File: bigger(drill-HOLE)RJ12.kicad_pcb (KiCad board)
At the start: 2 copper layers, 21.6 x 27.9 mm, 2 parts, among them J1 Conn_02x06_Top_Bottom, P1 RJ12_Housing

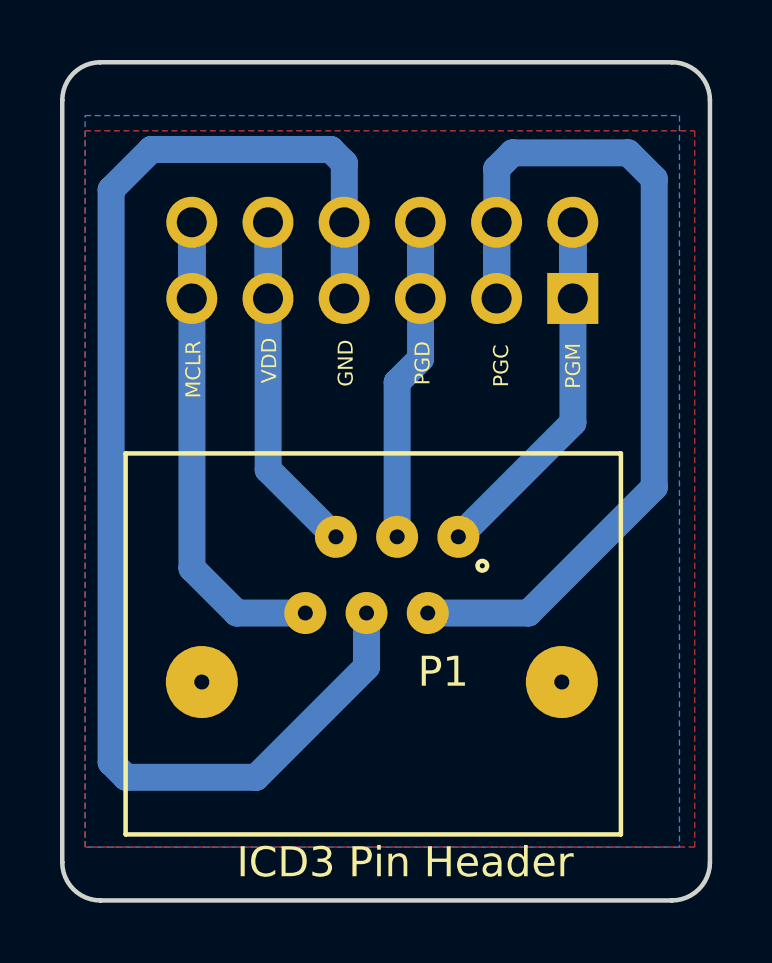
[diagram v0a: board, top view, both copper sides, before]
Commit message: Re-design the rj12 housing
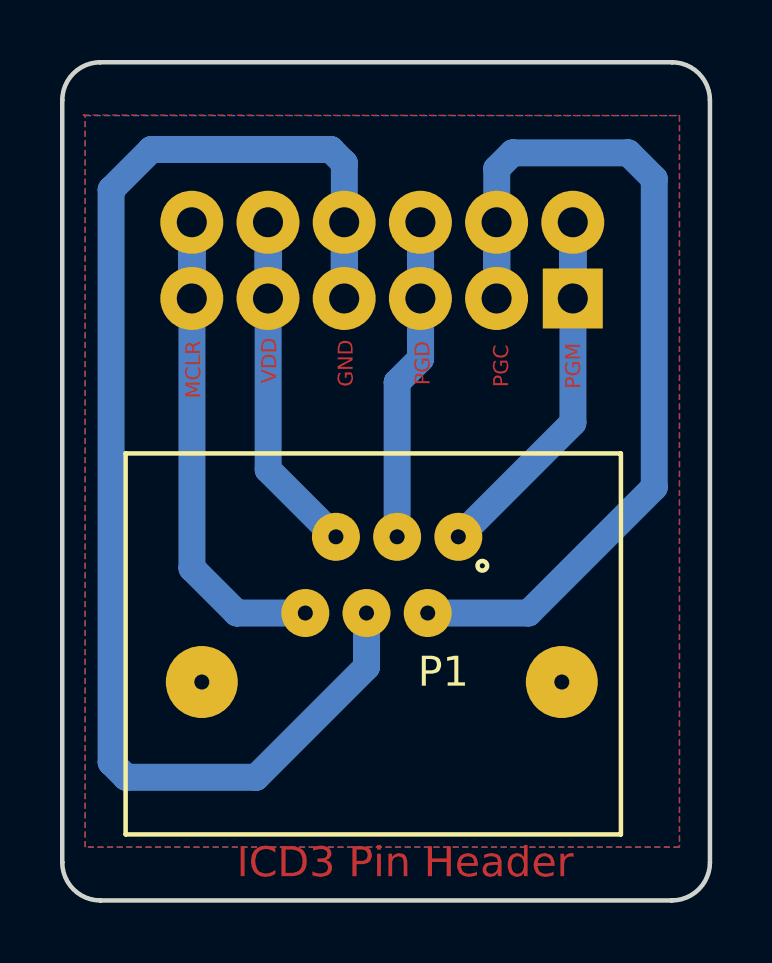
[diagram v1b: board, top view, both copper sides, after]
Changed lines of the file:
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@@
   (page A4)
   (layers
-    (0 F.Cu signal hide)
+    (0 F.Cu signal)
     (31 B.Cu signal)
     (32 B.Adhes user)
@@
     (mod_text_size 1 1)
     (mod_text_width 0.15)
-    (pad_size 1.7 1.7)
-    (pad_drill 1)
+    (pad_size 1.6 1.6)
+    (pad_drill 0.5)
     (pad_to_mask_clearance 0.2)
     (aux_axis_origin 44.45 16.51)
@@
     (pad "" np_thru_hole circle (at 8.55 2.3) (size 2.4 2.4) (drill 0.5) (layers *.Cu *.Mask))
     (pad "" np_thru_hole circle (at -3.45 2.3) (size 2.4 2.4) (drill 0.5) (layers *.Cu *.Mask))
-    (pad 1 thru_hole circle (at 5.1 -2.54) (size 1.4 1.4) (drill 0.5) (layers *.Cu *.Mask)
+    (pad 1 thru_hole circle (at 5.1 -2.54) (size 1.6 1.6) (drill 0.5) (layers *.Cu *.Mask)
       (net 6 pin1))
-    (pad 3 thru_hole circle (at 3.06 -2.54) (size 1.4 1.4) (drill 0.5) (layers *.Cu *.Mask)
+    (pad 3 thru_hole circle (at 3.06 -2.54) (size 1.6 1.6) (drill 0.5) (layers *.Cu *.Mask)
       (net 4 pin3))
-    (pad 5 thru_hole circle (at 1.02 -2.54) (size 1.4 1.4) (drill 0.5) (layers *.Cu *.Mask)
+    (pad 5 thru_hole circle (at 1.02 -2.54) (size 1.6 1.6) (drill 0.5) (layers *.Cu *.Mask)
       (net 1 pin5))
-    (pad 2 thru_hole circle (at 4.08 0) (size 1.4 1.4) (drill 0.5) (layers *.Cu *.Mask)
+    (pad 2 thru_hole circle (at 4.08 0) (size 1.6 1.6) (drill 0.5) (layers *.Cu *.Mask)
       (net 5 pin2))
-    (pad 4 thru_hole circle (at 2.04 0) (size 1.4 1.4) (drill 0.5) (layers *.Cu *.Mask)
+    (pad 4 thru_hole circle (at 2.04 0) (size 1.6 1.6) (drill 0.5) (layers *.Cu *.Mask)
       (net 3 pin4))
-    (pad 6 thru_hole circle (at 0 0) (size 1.4 1.4) (drill 0.5) (layers *.Cu *.Mask)
+    (pad 6 thru_hole circle (at 0 0) (size 1.6 1.6) (drill 0.5) (layers *.Cu *.Mask)
       (net 2 pin6))
   )
@@
       (effects (font (size 1 1) (thickness 0.15)) (justify mirror))
     )
-    (pad 1 thru_hole rect (at 0 0 90) (size 1.7 1.7) (drill 1) (layers *.Cu *.Mask)
+    (pad 1 thru_hole rect (at 0 0 90) (size 2 2) (drill 1) (layers *.Cu *.Mask)
       (net 6 pin1))
-    (pad 7 thru_hole oval (at 2.54 0 90) (size 1.7 1.7) (drill 1) (layers *.Cu *.Mask)
+    (pad 7 thru_hole oval (at 2.54 0 90) (size 2.1 2.1) (drill 1) (layers *.Cu *.Mask)
       (net 6 pin1))
-    (pad 2 thru_hole oval (at 0 -2.54 90) (size 1.7 1.7) (drill 1) (layers *.Cu *.Mask)
+    (pad 2 thru_hole oval (at 0 -2.54 90) (size 2.1 2.1) (drill 1) (layers *.Cu *.Mask)
       (net 5 pin2))
-    (pad 8 thru_hole oval (at 2.54 -2.54 90) (size 1.7 1.7) (drill 1) (layers *.Cu *.Mask)
+    (pad 8 thru_hole oval (at 2.54 -2.54 90) (size 2.1 2.1) (drill 1) (layers *.Cu *.Mask)
       (net 5 pin2))
-    (pad 3 thru_hole oval (at 0 -5.08 90) (size 1.7 1.7) (drill 1) (layers *.Cu *.Mask)
+    (pad 3 thru_hole oval (at 0 -5.08 90) (size 2.1 2.1) (drill 1) (layers *.Cu *.Mask)
       (net 4 pin3))
-    (pad 9 thru_hole oval (at 2.54 -5.08 90) (size 1.7 1.7) (drill 1) (layers *.Cu *.Mask)
+    (pad 9 thru_hole oval (at 2.54 -5.08 90) (size 2.1 2.1) (drill 1) (layers *.Cu *.Mask)
       (net 4 pin3))
-    (pad 4 thru_hole oval (at 0 -7.62 90) (size 1.7 1.7) (drill 1) (layers *.Cu *.Mask)
+    (pad 4 thru_hole oval (at 0 -7.62 90) (size 2.1 2.1) (drill 1) (layers *.Cu *.Mask)
       (net 3 pin4))
-    (pad 10 thru_hole oval (at 2.54 -7.62 90) (size 1.7 1.7) (drill 1) (layers *.Cu *.Mask)
+    (pad 10 thru_hole oval (at 2.54 -7.62 90) (size 2.1 2.1) (drill 1) (layers *.Cu *.Mask)
       (net 3 pin4))
-    (pad 5 thru_hole oval (at 0 -10.16 90) (size 1.7 1.7) (drill 1) (layers *.Cu *.Mask)
+    (pad 5 thru_hole oval (at 0 -10.16 90) (size 2.1 2.1) (drill 1) (layers *.Cu *.Mask)
       (net 1 pin5))
-    (pad 11 thru_hole oval (at 2.54 -10.16 90) (size 1.7 1.7) (drill 1) (layers *.Cu *.Mask)
+    (pad 11 thru_hole oval (at 2.54 -10.16 90) (size 2.1 2.1) (drill 1) (layers *.Cu *.Mask)
       (net 1 pin5))
-    (pad 6 thru_hole oval (at 0 -12.7 90) (size 1.7 1.7) (drill 1) (layers *.Cu *.Mask)
+    (pad 6 thru_hole oval (at 0 -12.7 90) (size 2.1 2.1) (drill 1) (layers *.Cu *.Mask)
       (net 2 pin6))
-    (pad 12 thru_hole oval (at 2.54 -12.7 90) (size 1.7 1.7) (drill 1) (layers *.Cu *.Mask)
+    (pad 12 thru_hole oval (at 2.54 -12.7 90) (size 2.1 2.1) (drill 1) (layers *.Cu *.Mask)
       (net 2 pin6))
     (model ${KISYS3DMOD}/Pin_Headers.3dshapes/Pin_Header_Straight_2x06_Pitch2.54mm.wrl
@@
     )
   )
-  (gr_text MCLR (at 25.96 26.75 90) (layer F.SilkS)
-    (effects (font (size 0.5 0.5) (thickness 0.125)))
-  )
-  (gr_text VDD (at 28.49 26.45 90) (layer F.SilkS)
-    (effects (font (size 0.5 0.5) (thickness 0.125)))
-  )
-  (gr_text GND (at 31.04 26.54 90) (layer F.SilkS)
-    (effects (font (size 0.5 0.5) (thickness 0.125)))
-  )
-  (gr_text PGD (at 33.6 26.54 90) (layer F.SilkS)
-    (effects (font (size 0.5 0.5) (thickness 0.125)))
-  )
-  (gr_text PGC (at 36.22 26.63 90) (layer F.SilkS)
-    (effects (font (size 0.5 0.5) (thickness 0.125)))
-  )
-  (gr_text PGM (at 38.62 26.63 90) (layer F.SilkS)
-    (effects (font (size 0.5 0.5) (thickness 0.125)))
-  )
-  (gr_text "ICD3 Pin Header" (at 33.02 43.18) (layer F.SilkS)
+  (gr_text MCLR (at 25.96 26.75 90) (layer F.Cu)
+    (effects (font (size 0.5 0.5) (thickness 0.125)))
+  )
+  (gr_text VDD (at 28.49 26.45 90) (layer F.Cu)
+    (effects (font (size 0.5 0.5) (thickness 0.125)))
+  )
+  (gr_text GND (at 31.04 26.54 90) (layer F.Cu)
+    (effects (font (size 0.5 0.5) (thickness 0.125)))
+  )
+  (gr_text PGD (at 33.6 26.54 90) (layer F.Cu)
+    (effects (font (size 0.5 0.5) (thickness 0.125)))
+  )
+  (gr_text PGC (at 36.22 26.63 90) (layer F.Cu)
+    (effects (font (size 0.5 0.5) (thickness 0.125)))
+  )
+  (gr_text PGM (at 38.62 26.63 90) (layer F.Cu)
+    (effects (font (size 0.5 0.5) (thickness 0.125)))
+  )
+  (gr_text "ICD3 Pin Header" (at 33.02 43.18) (layer F.Cu)
     (effects (font (size 1 1) (thickness 0.25)))
   )
@@
   (segment (start 37.13226 34.86912) (end 41.32326 30.67812) (width 0.9) (layer B.Cu) (net 5))
   (segment (start 38.61308 22.15642) (end 38.61308 24.69642) (width 0.9) (layer B.Cu) (net 6))
-  (segment (start 34.7926 32.32912) (end 34.8107 32.32912) (width 0.9) (layer F.Cu) (net 6))
+  (segment (start 34.7926 32.32912) (end 34.8107 32.32912) (width 0.25) (layer F.Cu) (net 6))
   (segment (start 34.8107 32.32912) (end 38.61308 28.52674) (width 0.9) (layer B.Cu) (net 6))
   (segment (start 38.61308 28.52674) (end 38.61308 22.15642) (width 0.9) (layer B.Cu) (net 6))
-  (zone (net 0) (net_name "") (layer F.Cu) (hatch edge 0.508)
-    (connect_pads (clearance 0.508))
-    (min_thickness 0.254)
-    (fill yes (arc_segments 16) (thermal_gap 0.508) (thermal_bridge_width 0.508))
-    (polygon
-      (pts
-        (xy 22.352 18.796) (xy 42.672 18.796) (xy 42.672 42.672) (xy 22.352 42.672)
-      )
-    )
-  )
   (zone (net 0) (net_name "") (layer B.Cu) (hatch edge 0.508)
     (connect_pads (clearance 0.508))
@@
       )
     )
+  )
+  (zone (net 0) (net_name "") (layer F.Cu) (hatch edge 0.508)
+    (connect_pads (clearance 0.508))
+    (min_thickness 0.254)
+    (fill yes (arc_segments 16) (thermal_gap 0.508) (thermal_bridge_width 0.508))
+    (polygon
+      (pts
+        (xy 22.28 18.27) (xy 42.164 18.288) (xy 42.164 42.672) (xy 22.352 42.672) (xy 22.352 18.288)
+        (xy 22.352 18.288)
+      )
+    )
